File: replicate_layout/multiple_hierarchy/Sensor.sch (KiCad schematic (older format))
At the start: 3 parts, among them U401 INA240

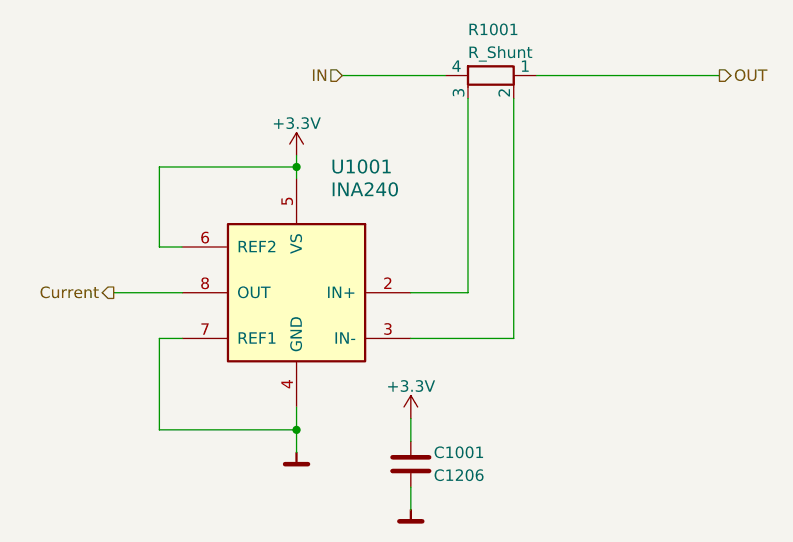
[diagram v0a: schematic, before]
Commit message: Changed test project to include complex hierarchy
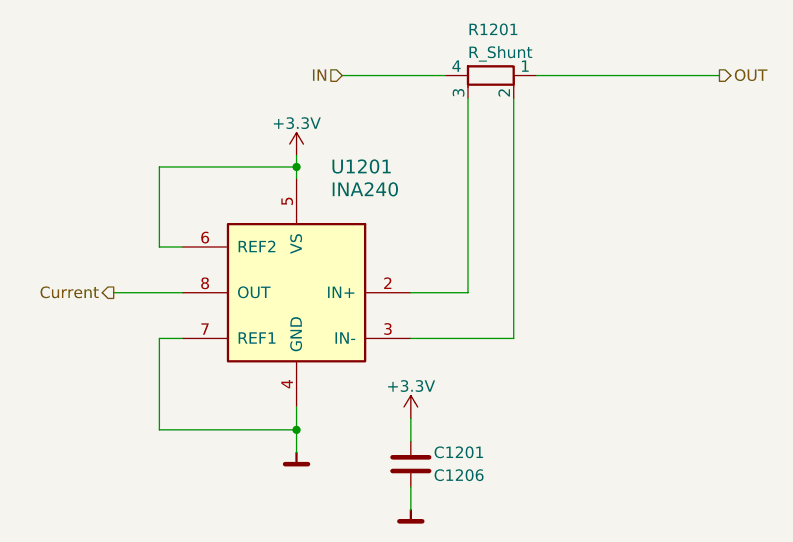
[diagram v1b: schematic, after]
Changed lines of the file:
@@
 $Descr A4 11693 8268
 encoding utf-8
-Sheet 4 10
+Sheet 4 13
 Title ""
 Date ""
@@
 P 2800 1750
 AR Path="/5B767FE4/5B767FF5/5B76BD36" Ref="R401"  Part="1"
-AR Path="/5B76D023/5B767FF5/5B76BD36" Ref="R701"  Part="1"
-AR Path="/5B76D031/5B767FF5/5B76BD36" Ref="R1001"  Part="1"
-F 0 "R1001" V 2600 1650 50  0000 L CNN
+AR Path="/5B76D023/5B767FF5/5B76BD36" Ref="R801"  Part="1"
+AR Path="/5B76D031/5B767FF5/5B76BD36" Ref="R1201"  Part="1"
+F 0 "R1201" V 2600 1650 50  0000 L CNN
 F 1 "R_Shunt" V 2700 1650 50  0000 L CNN
 F 2 "Passives:RM" V 2730 1750 50  0001 C CNN
@@
 P 1950 2700
 AR Path="/5B767FE4/5B767FF5/5B76BDE6" Ref="U401"  Part="1"
-AR Path="/5B76D023/5B767FF5/5B76BDE6" Ref="U701"  Part="1"
-AR Path="/5B76D031/5B767FF5/5B76BDE6" Ref="U1001"  Part="1"
-F 0 "U1001" H 1800 3250 60  0000 R CNN
+AR Path="/5B76D023/5B767FF5/5B76BDE6" Ref="U801"  Part="1"
+AR Path="/5B76D031/5B767FF5/5B76BDE6" Ref="U1201"  Part="1"
+F 0 "U1201" H 1800 3250 60  0000 R CNN
 F 1 "INA240" H 1800 3150 60  0000 R CNN
 F 2 "Package_SO:TSSOP-8_4.4x3mm_P0.65mm" H 2050 3300 60  0001 L CNN
@@
 P 1950 3400
 AR Path="/5B767FE4/5B767FF5/5B76BF5A" Ref="#PWR0402"  Part="1"
-AR Path="/5B76D023/5B767FF5/5B76BF5A" Ref="#PWR0702"  Part="1"
-AR Path="/5B76D031/5B767FF5/5B76BF5A" Ref="#PWR01002"  Part="1"
-F 0 "#PWR01002" H 1950 3250 50  0001 C CNN
+AR Path="/5B76D023/5B767FF5/5B76BF5A" Ref="#PWR0802"  Part="1"
+AR Path="/5B76D031/5B767FF5/5B76BF5A" Ref="#PWR01202"  Part="1"
+F 0 "#PWR01202" H 1950 3250 50  0001 C CNN
 F 1 "GND" H 2100 3350 50  0001 C CNN
 F 2 "" H 1950 3400 50  0001 C CNN
@@
 P 1950 2100
 AR Path="/5B767FE4/5B767FF5/5B76BFC7" Ref="#PWR0401"  Part="1"
-AR Path="/5B76D023/5B767FF5/5B76BFC7" Ref="#PWR0701"  Part="1"
-AR Path="/5B76D031/5B767FF5/5B76BFC7" Ref="#PWR01001"  Part="1"
-F 0 "#PWR01001" H 1950 1950 50  0001 C CNN
+AR Path="/5B76D023/5B767FF5/5B76BFC7" Ref="#PWR0801"  Part="1"
+AR Path="/5B76D031/5B767FF5/5B76BFC7" Ref="#PWR01201"  Part="1"
+F 0 "#PWR01201" H 1950 1950 50  0001 C CNN
 F 1 "+3.3V" H 1950 2240 50  0000 C CNN
 F 2 "" H 1950 2100 50  0001 C CNN
@@
 P 2450 3450
 AR Path="/5B767FE4/5B767FF5/5B76C4AF" Ref="C401"  Part="1"
-AR Path="/5B76D023/5B767FF5/5B76C4AF" Ref="C701"  Part="1"
-AR Path="/5B76D031/5B767FF5/5B76C4AF" Ref="C1001"  Part="1"
-F 0 "C1001" H 2550 3500 50  0000 L CNN
+AR Path="/5B76D023/5B767FF5/5B76C4AF" Ref="C801"  Part="1"
+AR Path="/5B76D031/5B767FF5/5B76C4AF" Ref="C1201"  Part="1"
+F 0 "C1201" H 2550 3500 50  0000 L CNN
 F 1 "C1206" H 2550 3400 50  0000 L CNN
 F 2 "Passives:C1206M" H 2500 3350 50  0001 L CNN
@@
 P 2450 3250
 AR Path="/5B767FE4/5B767FF5/5B76C9E1" Ref="#PWR0403"  Part="1"
-AR Path="/5B76D023/5B767FF5/5B76C9E1" Ref="#PWR0703"  Part="1"
-AR Path="/5B76D031/5B767FF5/5B76C9E1" Ref="#PWR01003"  Part="1"
-F 0 "#PWR01003" H 2450 3100 50  0001 C CNN
+AR Path="/5B76D023/5B767FF5/5B76C9E1" Ref="#PWR0803"  Part="1"
+AR Path="/5B76D031/5B767FF5/5B76C9E1" Ref="#PWR01203"  Part="1"
+F 0 "#PWR01203" H 2450 3100 50  0001 C CNN
 F 1 "+3.3V" H 2450 3390 50  0000 C CNN
 F 2 "" H 2450 3250 50  0001 C CNN
@@
 P 2450 3650
 AR Path="/5B767FE4/5B767FF5/5B76C9F2" Ref="#PWR0404"  Part="1"
-AR Path="/5B76D023/5B767FF5/5B76C9F2" Ref="#PWR0704"  Part="1"
-AR Path="/5B76D031/5B767FF5/5B76C9F2" Ref="#PWR01004"  Part="1"
-F 0 "#PWR01004" H 2450 3500 50  0001 C CNN
+AR Path="/5B76D023/5B767FF5/5B76C9F2" Ref="#PWR0804"  Part="1"
+AR Path="/5B76D031/5B767FF5/5B76C9F2" Ref="#PWR01204"  Part="1"
+F 0 "#PWR01204" H 2450 3500 50  0001 C CNN
 F 1 "GND" H 2600 3600 50  0001 C CNN
 F 2 "" H 2450 3650 50  0001 C CNN
